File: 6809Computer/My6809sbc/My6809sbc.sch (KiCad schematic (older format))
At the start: 57 parts, among them J1 HEADER 2x5, J10 TP3, J11 AUDIO OUT, J12 HEADER 2x20, J13 Conn_01x02, J2 HEADER 1x6, J3 HEADER 2x5, J4 HEADER 2x5, J5 TP1, J6 TP2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

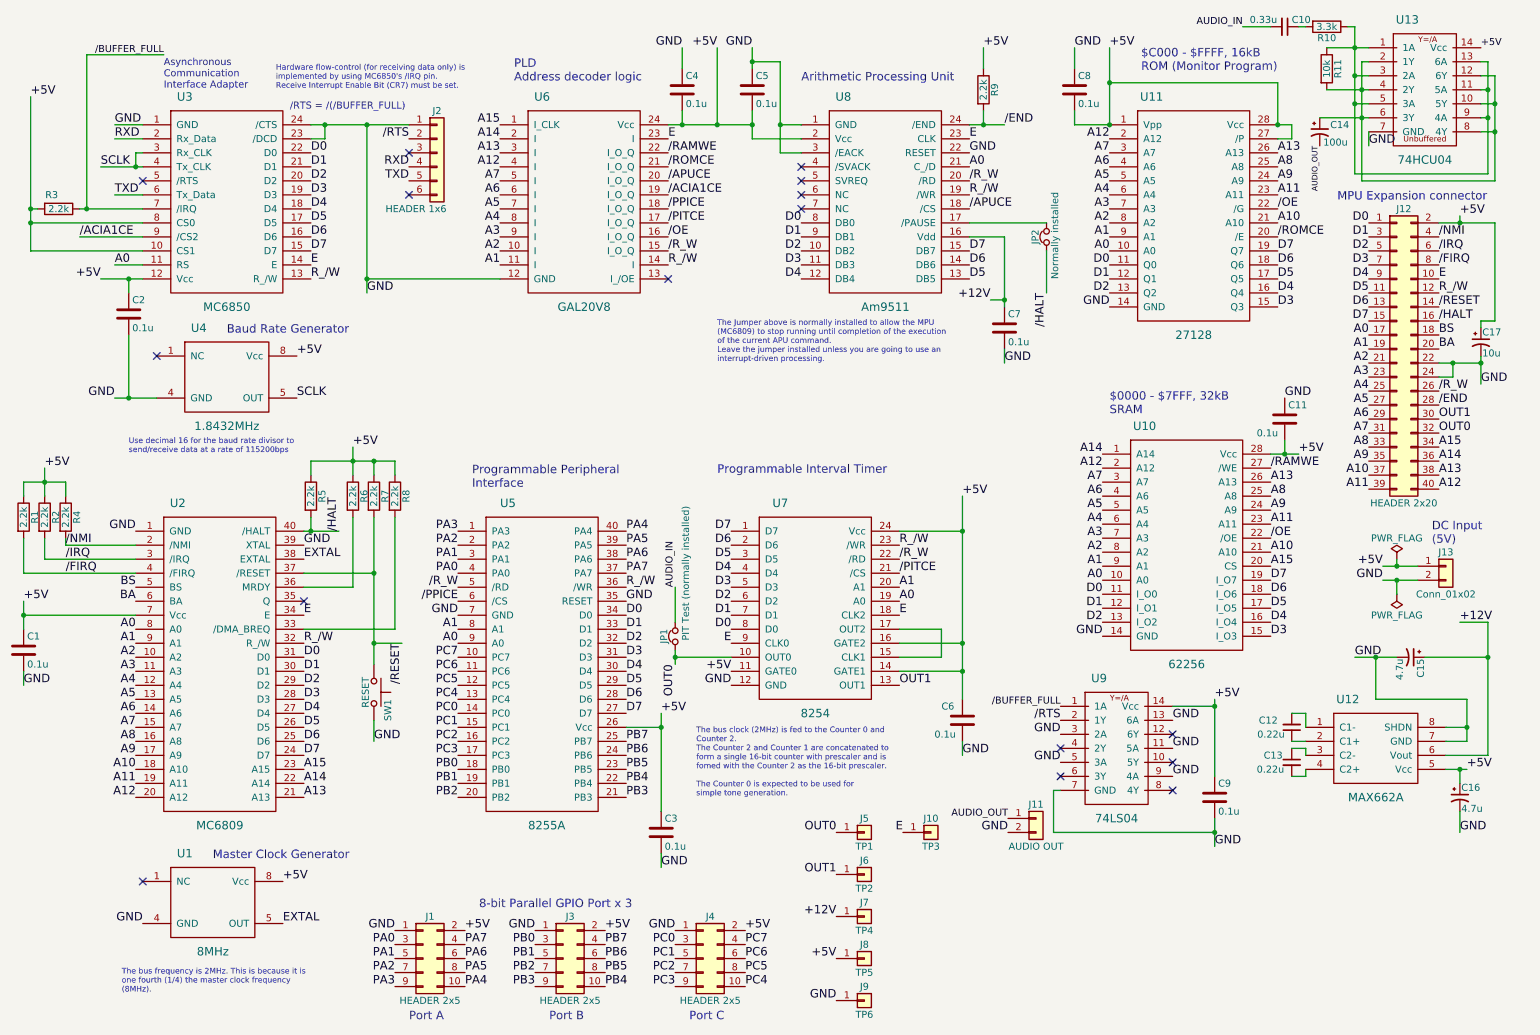
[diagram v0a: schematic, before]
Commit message: Update design files of 6809 SBC
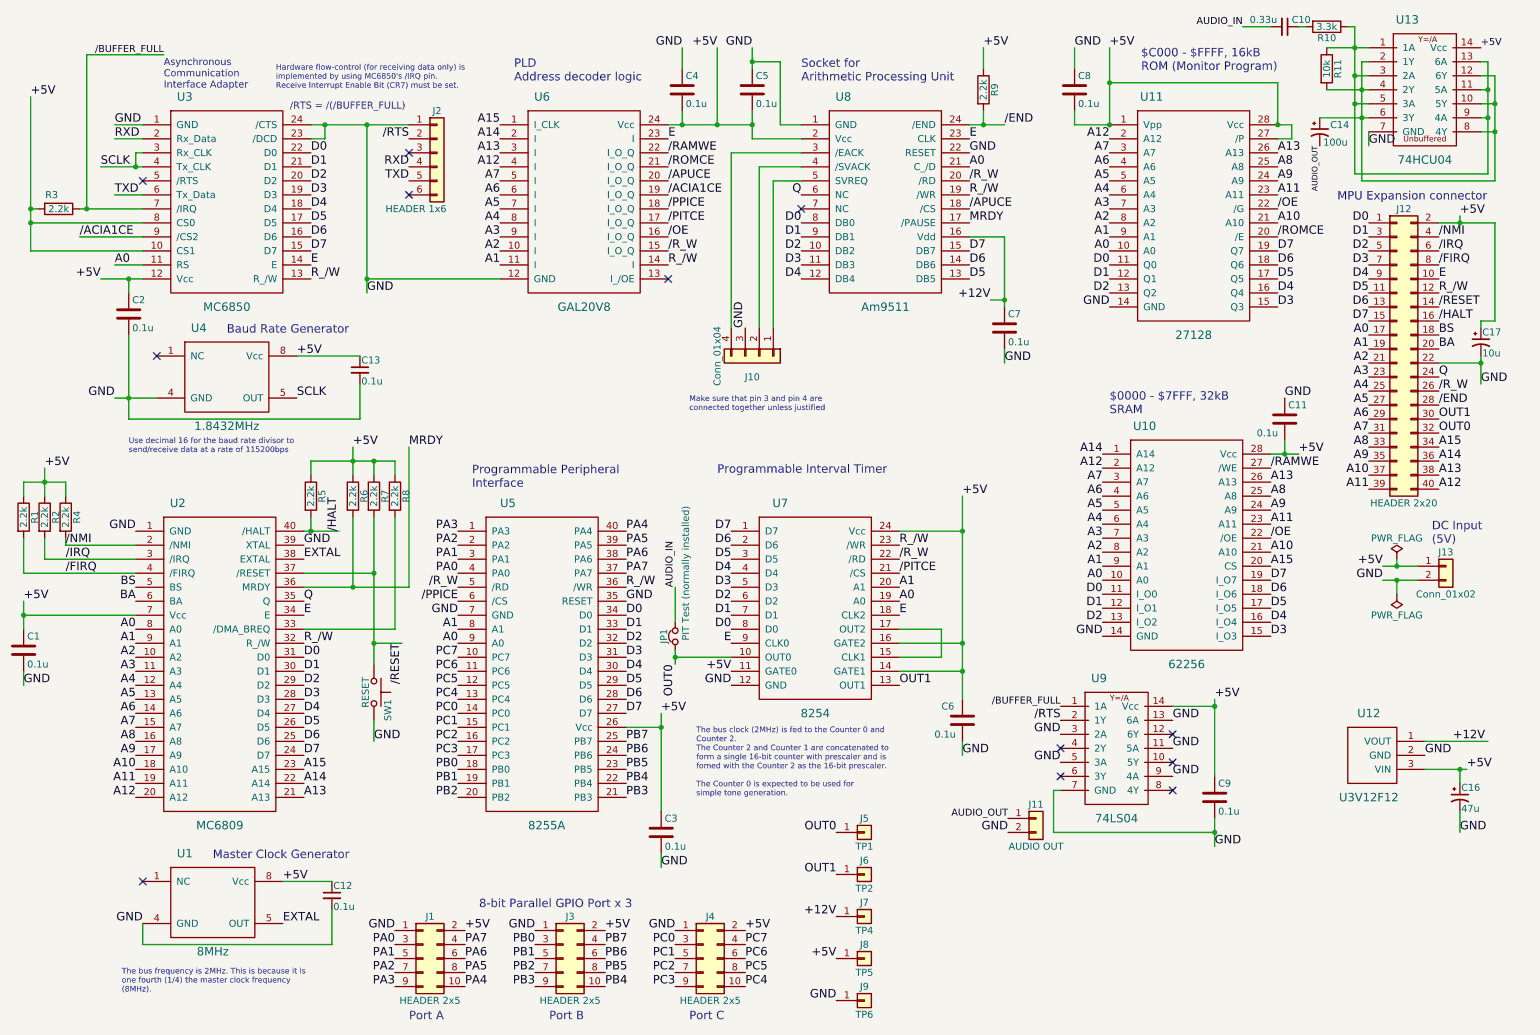
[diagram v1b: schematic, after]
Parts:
- removed C15: 4.7u, Capacitors_THT:CP_Radial_D5.0mm_P2.50mm, symbol CP1_Small
- removed J10: TP3, Pin_Headers:Pin_Header_Straight_1x01_Pitch2.54mm, symbol Conn_01x01
- removed JP2: Normally installed, Pin_Headers:Pin_Header_Straight_1x02_Pitch2.54mm, symbol Jumper_NC_Small
- removed U12: MAX662A, Housings_DIP:DIP-8_W7.62mm_Socket, symbol MAX662A
- added J10: Conn_01x04, Pin_Headers:Pin_Header_Straight_1x04_Pitch2.54mm, symbol Conn_01x04
- added U12: U3V12F12, Pin_Headers:Pin_Header_Straight_1x03_Pitch2.54mm, symbol U3V12F12
- C12, C13: value 0.22u -> 0.1u; footprint Capacitors_THT:C_Disc_D5.0mm_W2.5mm_P5.00mm -> Capacitors_THT:C_Disc_D5.0mm_W2.5mm_P2.50mm
- C16: value 4.7u -> 47u
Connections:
- net +12V: now also U12.1 (VOUT)
- net +5V: now also C12.1, C13.1, U12.3 (VIN)
- net GND: now also C12.2, C13.2, J10.3 (Pin_3), U12.2 (GND); no longer J12.24 (Pin_24), U8.3 (/EACK)
- net MRDY: now reaches U8.17 (/PAUSE)
- net MRDY: now also R6.2, U2.36 (MRDY)
- net at U8.4 (/SVACK): now also J10.2 (Pin_2)
- net at U8.5 (SVREQ): now also J10.1 (Pin_1)
- net Q: now reaches U8.6 (NC)
- net Q: now also J12.24 (Pin_24), U2.35 (Q)
- new net: J10.4 (Pin_4), U8.3 (/EACK)
- no-connect marks 16 -> 12
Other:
- note added: "Make sure that pin 3 and pin 4 are \nconnected together unless justified"
- note added: "Socket for\nArithmetic Processing Unit"
- note removed: "Arithmetic Processing Unit"
- note removed: "The Jumper above is normally installed to allow the MPU \n(MC6809) to stop running until completion of the execution \nof the current APU command.\nLeave the jumper installed unless you are going to use an \ninterrupt-driven processing."
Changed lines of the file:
@@
 Sheet 1 1
 Title "MUTIF09 6809 Single Board Computer"
-Date "2018-07-01"
-Rev "1"
+Date "2018-09-10"
+Rev "2"
 Comp "MUTIF09 Project"
 Comment1 ""
@@
 	1    0    0    -1
 $EndComp
-NoConn ~ 6200 1800
 NoConn ~ 6200 1900
 $Comp
@@
 F 3 "" H 10450 2900 50  0001 C CNN
 	1    10450 2900
-	1    0    0    -1
-$EndComp
-$Comp
-L MAX662A U12
-U 1 1 5B2A6291
-P 10300 5750
-F 0 "U12" H 10100 6100 60  0000 C CNN
-F 1 "MAX662A" H 10300 5400 60  0000 C CNN
-F 2 "Housings_DIP:DIP-8_W7.62mm_Socket" H 10300 5300 60  0001 C CNN
-F 3 "" H 10300 5300 60  0001 C CNN
-	1    10300 5750
 	1    0    0    -1
 $EndComp
@@
 NoConn ~ 8850 5850
 NoConn ~ 8850 6050
-Text Label 10150 5100 0    60   ~ 0
+Text Label 10650 5800 0    60   ~ 0
 GND
 Text Label 10950 5900 0    60   ~ 0
 +5V
-Text Label 10900 4850 0    60   ~ 0
+Text Label 10850 5700 0    60   ~ 0
 +12V
 $Comp
@@
 Text Label 10750 2700 0    60   ~ 0
 /HALT
-NoConn ~ 2650 4700
 Text Notes 1400 3650 0    40   ~ 0
 Use decimal 16 for the baud rate divisor to\nsend/receive data at a rate of 115200bps
@@
 Text Notes 3850 3900 0    60   ~ 0
 Programmable Peripheral\nInterface
-NoConn ~ 6200 1600
-NoConn ~ 6200 1700
 $Comp
 L R R9
@@
 Text Label 10750 3300 0    60   ~ 0
 /END
-$Comp
-L Jumper_NC_Small JP2
-U 1 1 5B2EC48C
-P 7950 2100
-F 0 "JP2" H 7950 2180 50  0000 C CNN
-F 1 "Normally installed" H 7960 2040 50  0000 C CNN
-F 2 "Pin_Headers:Pin_Header_Straight_1x02_Pitch2.54mm" H 7950 2100 50  0001 C CNN
-F 3 "" H 7950 2100 50  0001 C CNN
-	1    7950 2100
-	0    -1   -1   0
-$EndComp
-Text Label 7950 2500 3    60   ~ 0
-/HALT
 Text Notes 6200 1000 0    60   ~ 0
-Arithmetic Processing Unit
+         Socket for\nArithmetic Processing Unit
 NoConn ~ 8050 5950
 Text Notes 4150 1000 0    60   ~ 0
@@
 Text Label 6450 6350 2    60   ~ 0
 OUT0
-$Comp
-L Conn_01x01 J10
-U 1 1 5B30BF3F
-P 7125 6350
-F 0 "J10" H 7125 6450 50  0000 C CNN
-F 1 "TP3" H 7125 6250 50  0000 C CNN
-F 2 "Pin_Headers:Pin_Header_Straight_1x01_Pitch2.54mm" H 7125 6350 50  0001 C CNN
-F 3 "" H 7125 6350 50  0001 C CNN
-	1    7125 6350
-	1    0    0    -1
-$EndComp
 Text Label 9550 4450 0    60   ~ 0
 A15
@@
 Text Notes 5400 7700 0    60   ~ 0
 Port C
-Text Notes 5600 3000 0    40   ~ 0
-The Jumper above is normally installed to allow the MPU \n(MC6809) to stop running until completion of the execution \nof the current APU command.\nLeave the jumper installed unless you are going to use an \ninterrupt-driven processing.
 $Comp
 L 74HCU04 U13
@@
 Text Label 7675 6250 2    50   ~ 0
 AUDIO_OUT
-Text Label 6925 6350 2    60   ~ 0
-E
 $Comp
 L C_Small C10
@@
 GND
 $Comp
-L C_Small C12
-U 1 1 5B315BD3
-P 9700 5600
-F 0 "C12" H 9800 5550 50  0000 L CNN
-F 1 "0.22u" H 9750 5650 50  0000 L CNN
-F 2 "Capacitors_THT:C_Disc_D5.0mm_W2.5mm_P5.00mm" H 9700 5600 50  0001 C CNN
-F 3 "" H 9700 5600 50  0001 C CNN
-	1    9700 5600
-	-1   0    0    1
-$EndComp
-$Comp
-L C_Small C13
-U 1 1 5B315C78
-P 9700 5850
-F 0 "C13" H 9500 5900 50  0000 L CNN
-F 1 "0.22u" H 9450 5800 50  0000 L CNN
-F 2 "Capacitors_THT:C_Disc_D5.0mm_W2.5mm_P5.00mm" H 9700 5850 50  0001 C CNN
-F 3 "" H 9700 5850 50  0001 C CNN
-	1    9700 5850
-	1    0    0    -1
-$EndComp
-$Comp
-L CP1_Small C15
-U 1 1 5B317098
-P 10550 5100
-F 0 "C15" H 10560 5170 50  0000 L CNN
-F 1 "4.7u" H 10560 5020 50  0000 L CNN
-F 2 "Capacitors_THT:CP_Radial_D5.0mm_P2.50mm" H 10550 5100 50  0001 C CNN
-F 3 "" H 10550 5100 50  0001 C CNN
-	1    10550 5100
-	0    1    1    0
-$EndComp
-$Comp
 L CP1_Small C16
 U 1 1 5B3174A7
 P 10900 6100
 F 0 "C16" H 10910 6170 50  0000 L CNN
-F 1 "4.7u" H 10910 6020 50  0000 L CNN
+F 1 "47u" H 10910 6020 50  0000 L CNN
 F 2 "Capacitors_THT:CP_Radial_D5.0mm_P2.50mm" H 10900 6100 50  0001 C CNN
 F 3 "" H 10900 6100 50  0001 C CNN
@@
 Text Label 1300 1300 0    60   ~ 0
 GND
+Text Label 1450 4600 2    60   ~ 0
+BS
+Text Label 1450 4700 2    60   ~ 0
+BA
+Text Label 3400 3600 0    60   ~ 0
+MRDY
+Text Label 7400 2000 0    60   ~ 0
+MRDY
+Text Label 10750 3100 0    60   ~ 0
+Q
+Text Label 2650 4700 0    60   ~ 0
+Q
+$Comp
+L C_Small C13
+U 1 1 5B96DFFE
+P 3050 3050
+F 0 "C13" H 3060 3120 50  0000 L CNN
+F 1 "0.1u" H 3060 2970 50  0000 L CNN
+F 2 "Capacitors_THT:C_Disc_D5.0mm_W2.5mm_P2.50mm" H 3050 3050 50  0001 C CNN
+F 3 "" H 3050 3050 50  0001 C CNN
+	1    3050 3050
+	1    0    0    -1
+$EndComp
+$Comp
+L C_Small C12
+U 1 1 5B96EE63
+P 2850 6800
+F 0 "C12" H 2860 6870 50  0000 L CNN
+F 1 "0.1u" H 2860 6720 50  0000 L CNN
+F 2 "Capacitors_THT:C_Disc_D5.0mm_W2.5mm_P2.50mm" H 2850 6800 50  0001 C CNN
+F 3 "" H 2850 6800 50  0001 C CNN
+	1    2850 6800
+	1    0    0    -1
+$EndComp
+$Comp
+L U3V12F12 U12
+U 1 1 5B973F86
+P 10300 5800
+F 0 "U12" H 10250 6100 60  0000 C CNN
+F 1 "U3V12F12" H 10250 5500 60  0000 C CNN
+F 2 "Pin_Headers:Pin_Header_Straight_1x03_Pitch2.54mm" H 10300 5800 60  0001 C CNN
+F 3 "" H 10300 5800 60  0001 C CNN
+	1    10300 5800
+	1    0    0    -1
+$EndComp
 Wire Wire Line
 	2700 1300 3400 1300
@@
 Wire Wire Line
 	6200 1300 6050 1300
-Wire Wire Line
-	6050 850  6050 1500
 Wire Wire Line
 	6050 850  5850 850
@@
 Connection ~ 7650 2550
 Wire Wire Line
-	10800 5900 10950 5900
-Wire Wire Line
-	10900 6000 10900 5900
-Connection ~ 10900 5900
-Wire Wire Line
-	10150 5100 10450 5100
-Wire Wire Line
-	10300 5100 10300 5400
-Wire Wire Line
-	10300 5400 10950 5400
-Wire Wire Line
-	10950 5400 10950 5700
-Wire Wire Line
-	10950 5600 10800 5600
-Connection ~ 10300 5100
-Wire Wire Line
-	10950 5700 10800 5700
-Connection ~ 10950 5600
-Wire Wire Line
-	11100 5800 10800 5800
-Wire Wire Line
-	11100 4850 11100 5800
-Wire Wire Line
-	11100 4850 10900 4850
-Wire Wire Line
-	10650 5100 11100 5100
-Connection ~ 11100 5100
-Wire Wire Line
 	1100 800  1650 800
 Wire Wire Line
@@
 Connection ~ 3150 4500
 Wire Wire Line
-	2650 4600 3000 4600
+	2650 4600 3400 4600
 Wire Wire Line
 	3000 4600 3000 4100
@@
 Wire Wire Line
 	10750 3000 11050 3000
-Wire Wire Line
-	10750 3100 10850 3100
-Wire Wire Line
-	10850 3100 10850 3000
-Connection ~ 10850 3000
 Connection ~ 11050 3000
 Wire Wire Line
@@
 	7200 5100 6900 5100
 Wire Wire Line
-	6050 1500 6200 1500
-Connection ~ 6050 1300
-Wire Wire Line
 	7500 750  7500 900
 Wire Wire Line
@@
 	7500 1200 7500 1300
 Connection ~ 7500 1300
-Wire Wire Line
-	7950 2200 7950 2500
-Wire Wire Line
-	7400 2000 7950 2000
 Connection ~ 700  2000
 Wire Wire Line
@@
 Connection ~ 5300 5100
 Wire Wire Line
-	9700 5500 9800 5500
-Wire Wire Line
-	9800 5500 9800 5600
-Wire Wire Line
-	9700 5700 9800 5700
-Wire Wire Line
-	9700 5750 9800 5750
-Wire Wire Line
-	9800 5750 9800 5800
-Wire Wire Line
-	9700 5950 9800 5950
-Wire Wire Line
-	9800 5950 9800 5900
-Wire Wire Line
 	10900 6200 10900 6350
 Wire Wire Line
 	1300 1300 1500 1300
 Wire Wire Line
-	1400 3250 1400 2800
+	1400 2800 1400 3400
 Wire Wire Line
 	1400 2500 1400 2400
@@
 Wire Wire Line
 	1500 1400 1300 1400
-Text Label 1450 4600 2    60   ~ 0
-BS
-Text Label 1450 4700 2    60   ~ 0
-BA
 Wire Wire Line
 	650  5200 650  5300
@@
 	6900 4200 7350 4200
 Connection ~ 7350 4200
+Connection ~ 3000 4600
+Wire Wire Line
+	3400 4600 3400 3600
+Wire Wire Line
+	3050 2950 2600 2950
+Wire Wire Line
+	3050 3150 3050 3400
+Wire Wire Line
+	2850 6700 2500 6700
+Wire Wire Line
+	2850 6900 2850 7150
+Wire Wire Line
+	1500 7000 1500 7150
+Wire Wire Line
+	1500 7150 2850 7150
+Wire Wire Line
+	3050 3400 1400 3400
+Wire Wire Line
+	10650 5700 11100 5700
+Wire Wire Line
+	10650 5900 10950 5900
+Wire Wire Line
+	10900 6000 10900 5900
+Connection ~ 10900 5900
+Wire Wire Line
+	5900 1600 6200 1600
+Wire Wire Line
+	6000 1700 6200 1700
+Wire Wire Line
+	6050 1300 6050 850
+Wire Wire Line
+	6200 1500 5700 1500
+Wire Wire Line
+	5700 1500 5700 2750
+Wire Wire Line
+	5900 2750 5900 1600
+Wire Wire Line
+	6000 2750 6000 1700
+Text Label 5800 2750 1    60   ~ 0
+GND
+Text Notes 5400 3350 0    40   ~ 0
+Make sure that pin 3 and pin 4 are \nconnected together unless justified
+Text Label 6200 1800 2    60   ~ 0
+Q
+$Comp
+L Conn_01x04 J10
+U 1 1 5B99B0DD
+P 5900 2950
+F 0 "J10" V 6050 2900 50  0000 C CNN
+F 1 "Conn_01x04" H 5900 2650 50  0000 C CNN
+F 2 "Pin_Headers:Pin_Header_Straight_1x04_Pitch2.54mm" H 5900 2950 50  0001 C CNN
+F 3 "" H 5900 2950 50  0001 C CNN
+	1    5900 2950
+	0    1    1    0
+$EndComp
 $EndSCHEMATC
